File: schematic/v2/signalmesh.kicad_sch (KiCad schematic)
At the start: 164 parts, among them J1 FPGA I/O, J10 INA219_CONFIG, J11 INA219_CONFIG, J12 AAM_DBG, J13 UUM_DBG, J14 ACM_DBG, J15 INA219_CONFIG, J16 DSM_DBG, J17 LCD_display, J18 LCD_display, J19 AudioJack3, J2 FPGA I/O, J20 USB3_A, J21 USB_A, J23 USB_A, J3 LCD_display, J4 TDM_DBG, J5 INA219_CONFIG, J6 INA219_CONFIG, J7 INA219_CONFIG, J8 FPGA I/O, J9 FPGA I/O, U1 NUCLEO-H753ZI, U10 INA219AxD, U11 INA219AxD, U12 INA219AxD, U13 INA219AxD, U14 W25Q128JVS, U15 AP2112K-3.3, U16 74HC4050D, U17 NUCLEO-H753ZI, U18 HDSP-7503, U19 HDSP-7503, U2 HDSP-7503, U20 INA219AxD, U21 74HC4050D, U22 AP2112K-3.3, U23 W25Q128JVS, U24 74HC4050D, U25 AP2112K-3.3, U26 W25Q128JVS, U27 MCP2551-I-P, U28 74LVC1G3157, U29 MCP2551-I-P, U3 NUCLEO-F303RE, U30 MCP2551-I-P, U31 MCP2551-I-P, U32 CH340G, U4 YAAJ_BluePill_Part_Like, U5 24LC256-I_SN, U6 BME280, U7 INA219AxD, U8 24LC256-I_SN, U9 NUCLEO-F446RE, Y1 Crystal

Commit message: i should really make this multiple sheets
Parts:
- added D37: LED_PWR, LED_SMD:LED_0603_1608Metric, symbol Device:LED
- added J22: USB_A, Connector_USB:USB_A_CNCTech_1001-011-01101_Horizontal, symbol Connector:USB_A
- added R56: 300, Resistor_SMD:R_0805_2012Metric_Pad1.20x1.40mm_HandSolder, symbol Device:R
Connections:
- net AAM_USB_D+: now also J22.3 (D+)
- net AAM_USB_D-: now also J22.2 (D-)
- net AAM_VDD: now also J22.1 (VBUS), R56.2
- net GND: now also D37.1 (K), J22.4 (GND)
- new net: D37.2 (A), R56.1

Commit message: removing the courtyard from the filler plots. theyre not actually components just an outline with throughholes
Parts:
- removed J20: USB3_A, Connector_USB:USB3_A_Plug_Wuerth_692112030100_Horizontal, symbol Connector:USB3_A
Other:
- note added: "MEDIA USB2.0 INPUT"
- moved on the sheet: D32, J21, R50
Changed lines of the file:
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@@
 	)
 	(rectangle
-		(start 332.74 173.99)
-		(end 377.19 209.55)
+		(start 180.34 232.41)
+		(end 224.79 267.97)
 		(stroke
 			(width 0)
@@
 		)
 	)
-	(text "MIDI USB2.0 INPUT"
+	(text "MEDIA USB2.0 INPUT"
 		(exclude_from_sim no)
 		(at 355.6 449.072 0)
@@
 	(text "MIDI USB2.0 INPUT"
 		(exclude_from_sim no)
-		(at 354.33 176.022 0)
+		(at 201.93 234.442 0)
 		(effects
 			(font
@@
 	)
 	(junction
-		(at 359.41 186.69)
+		(at 207.01 245.11)
 		(diameter 0)
 		(color 0 0 0 0)
@@
 	)
 	(junction
-		(at 349.25 203.2)
+		(at 196.85 261.62)
 		(diameter 0)
 		(color 0 0 0 0)
@@
 	(wire
 		(pts
-			(xy 349.25 203.2) (xy 349.25 201.93)
+			(xy 196.85 261.62) (xy 196.85 260.35)
 		)
 		(stroke
@@
 	(wire
 		(pts
-			(xy 337.82 203.2) (xy 337.82 200.66)
+			(xy 185.42 261.62) (xy 185.42 259.08)
 		)
 		(stroke
@@
 	(wire
 		(pts
-			(xy 349.25 203.2) (xy 337.82 203.2)
+			(xy 196.85 261.62) (xy 185.42 261.62)
 		)
 		(stroke
@@
 	(wire
 		(pts
-			(xy 359.41 181.61) (xy 359.41 186.69)
+			(xy 207.01 240.03) (xy 207.01 245.11)
 		)
 		(stroke
@@
 	(wire
 		(pts
-			(xy 359.41 186.69) (xy 356.87 186.69)
+			(xy 207.01 245.11) (xy 204.47 245.11)
 		)
 		(stroke
@@
 	(wire
 		(pts
-			(xy 359.41 181.61) (xy 337.82 181.61)
+			(xy 207.01 240.03) (xy 185.42 240.03)
 		)
 		(stroke
@@
 	(wire
 		(pts
-			(xy 337.82 181.61) (xy 337.82 185.42)
+			(xy 185.42 240.03) (xy 185.42 243.84)
 		)
 		(stroke
@@
 	(wire
 		(pts
-			(xy 359.41 186.69) (xy 361.95 186.69)
+			(xy 207.01 245.11) (xy 209.55 245.11)
 		)
 		(stroke
@@
 	(global_label "AAM_USB_D-"
 		(shape bidirectional)
-		(at 356.87 194.31 0)
+		(at 204.47 252.73 0)
 		(fields_autoplaced yes)
 		(effects
@@
 		)
 		(property "Intersheetrefs" "${INTERSHEET_REFS}"
-			(at 373.1827 194.31 0)
+			(at 220.7827 252.73 0)
 			(effects
 				(font
@@
 	(global_label "AAM_USB_D+"
 		(shape bidirectional)
-		(at 356.87 191.77 0)
+		(at 204.47 250.19 0)
 		(fields_autoplaced yes)
 		(effects
@@
 		)
 		(property "Intersheetrefs" "${INTERSHEET_REFS}"
-			(at 373.1827 191.77 0)
+			(at 220.7827 250.19 0)
 			(effects
 				(font
@@
 	(global_label "AAM_VDD"
 		(shape input)
-		(at 361.95 186.69 0)
+		(at 209.55 245.11 0)
 		(fields_autoplaced yes)
 		(effects
@@
 		)
 		(property "Intersheetrefs" "${INTERSHEET_REFS}"
-			(at 373.16 186.69 0)
+			(at 220.76 245.11 0)
 			(effects
 				(font
@@
 	(symbol
 		(lib_id "Connector:USB_A")
-		(at 349.25 191.77 0)
+		(at 196.85 250.19 0)
 		(unit 1)
 		(exclude_from_sim no)
@@
 		(fields_autoplaced yes)
 		(property "Reference" "J21"
-			(at 349.25 179.07 0)
+			(at 196.85 237.49 0)
 			(effects
 				(font
@@
 		)
 		(property "Value" "USB_A"
-			(at 349.25 181.61 0)
+			(at 196.85 240.03 0)
 			(effects
 				(font
@@
 		)
 		(property "Footprint" "Connector_USB:USB_A_CNCTech_1001-011-01101_Horizontal"
-			(at 353.06 193.04 0)
+			(at 200.66 251.46 0)
 			(effects
 				(font
@@
 		)
 		(property "Datasheet" "~"
-			(at 353.06 193.04 0)
+			(at 200.66 251.46 0)
 			(effects
 				(font
@@
 		)
 		(property "Description" "USB Type A connector"
-			(at 349.25 191.77 0)
+			(at 196.85 250.19 0)
 			(effects
 				(font
@@
 	(symbol
 		(lib_id "power:GND")
-		(at 349.25 203.2 0)
+		(at 196.85 261.62 0)
 		(unit 1)
 		(exclude_from_sim no)
@@
 		(fields_autoplaced yes)
 		(property "Reference" "#PWR0132"
-			(at 349.25 209.55 0)
+			(at 196.85 267.97 0)
 			(effects
 				(font
@@
 		)
 		(property "Value" "GND"
-			(at 349.25 208.28 0)
+			(at 196.85 266.7 0)
 			(effects
 				(font
@@
 		)
 		(property "Footprint" ""
-			(at 349.25 203.2 0)
+			(at 196.85 261.62 0)
 			(effects
 				(font
@@
 		)
 		(property "Datasheet" ""
-			(at 349.25 203.2 0)
+			(at 196.85 261.62 0)
 			(effects
 				(font
@@
 		)
 		(property "Description" "Power symbol creates a global label with name \"GND\" , ground"
-			(at 349.25 203.2 0)
+			(at 196.85 261.62 0)
 			(effects
 				(font
@@
 	)
 	(symbol
-		(lib_id "Connector:USB3_A")
-		(at 38.1 93.98 0)
-		(unit 1)
-		(exclude_from_sim no)
-		(in_bom yes)
-		(on_board yes)
-		(dnp no)
-		(fields_autoplaced yes)
-		(property "Reference" "J20"
-			(at 38.1 74.93 0)
-			(effects
-				(font
-					(size 1.27 1.27)
-				)
-			)
-		)
-		(property "Value" "USB3_A"
-			(at 38.1 77.47 0)
-			(effects
-				(font
-					(size 1.27 1.27)
-				)
-			)
-		)
-		(property "Footprint" "Connector_USB:USB3_A_Plug_Wuerth_692112030100_Horizontal"
-			(at 41.91 91.44 0)
-			(effects
-				(font
-					(size 1.27 1.27)
-				)
-				(hide yes)
-			)
-		)
-		(property "Datasheet" "~"
-			(at 41.91 91.44 0)
-			(effects
-				(font
-					(size 1.27 1.27)
-				)
-				(hide yes)
-			)
-		)
-		(property "Description" "USB 3.0 A connector"
-			(at 38.1 93.98 0)
-			(effects
-				(font
-					(size 1.27 1.27)
-				)
-				(hide yes)
-			)
-		)
-		(pin "6"
-		)
-		(pin "9"
-		)
-		(pin "1"
-		)
-		(pin "2"
-		)
-		(pin "3"
-		)
-		(pin "5"
-		)
-		(pin "4"
-		)
-		(pin "7"
-		)
-		(pin "10"
-		)
-		(pin "8"
-		)
-		(instances
-			(project ""
-				(path "/fe7b15e9-f0ed-4338-9f03-dd7651dace13"
-					(reference "J20")
-					(unit 1)
-				)
-			)
-		)
-	)
-	(symbol
 		(lib_id "Device:C_Small")
 		(at 593.09 29.21 90)
@@
 	(symbol
 		(lib_id "Device:R")
-		(at 337.82 189.23 180)
+		(at 185.42 247.65 180)
 		(unit 1)
 		(exclude_from_sim no)
@@
 		(fields_autoplaced yes)
 		(property "Reference" "R50"
-			(at 340.36 187.9599 0)
+			(at 187.96 246.3799 0)
 			(effects
 				(font
@@
 		)
 		(property "Value" "300"
-			(at 340.36 190.4999 0)
+			(at 187.96 248.9199 0)
 			(effects
 				(font
@@
 		)
 		(property "Footprint" "Resistor_SMD:R_0805_2012Metric_Pad1.20x1.40mm_HandSolder"
-			(at 339.598 189.23 90)
+			(at 187.198 247.65 90)
 			(effects
 				(font
@@
 		)
 		(property "Datasheet" "~"
-			(at 337.82 189.23 0)
+			(at 185.42 247.65 0)
 			(effects
 				(font
@@
 		)
 		(property "Description" "Resistor"
-			(at 337.82 189.23 0)
+			(at 185.42 247.65 0)
 			(effects
 				(font
@@
 		)
 		(property "DigiKey_Part_Number" "311-10.0KCRCT-ND"
-			(at 337.82 189.23 0)
+			(at 185.42 247.65 0)
 			(effects
 				(font
@@
 		)
 		(property "Price" "0.0129"
-			(at 337.82 189.23 0)
+			(at 185.42 247.65 0)
 			(effects
 				(font
@@
 	(symbol
 		(lib_id "Device:LED")
-		(at 337.82 196.85 90)
+		(at 185.42 255.27 90)
 		(unit 1)
 		(exclude_from_sim no)
@@
 		(fields_autoplaced yes)
 		(property "Reference" "D32"
-			(at 341.63 197.1674 90)
+			(at 189.23 255.5874 90)
 			(effects
 				(font
@@
 		)
 		(property "Value" "LED_PWR"
-			(at 341.63 199.7074 90)
+			(at 189.23 258.1274 90)
 			(effects
 				(font
@@
 		)
 		(property "Footprint" "LED_SMD:LED_0603_1608Metric"
-			(at 337.82 196.85 0)
+			(at 185.42 255.27 0)
 			(effects
 				(font
@@
 		)
 		(property "Datasheet" "~"
-			(at 337.82 196.85 0)
+			(at 185.42 255.27 0)
 			(effects
 				(font
@@
 		)
 		(property "Description" "Light emitting diode"
-			(at 337.82 196.85 0)
+			(at 185.42 255.27 0)
 			(effects
 				(font
@@
 		)
 		(property "Sim.Pins" "1=K 2=A"
-			(at 337.82 196.85 0)
+			(at 185.42 255.27 0)
 			(effects
 				(font

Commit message: moving to multiple sheets for the schematic
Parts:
- removed C11, C12, C13: 22pf, Capacitor_SMD:C_0805_2012Metric, symbol Device:C_Small
- removed D15, D21, D32, D33, D34, D37: LED_PWR, LED_SMD:LED_0603_1608Metric, symbol Device:LED
- removed D16, D22: LED_OK, LED_SMD:LED_0603_1608Metric, symbol Device:LED
- removed D17, D23: LED_FAIL, LED_SMD:LED_0603_1608Metric, symbol Device:LED
- removed D18, D24: LED_WARN, LED_SMD:LED_0603_1608Metric, symbol Device:LED
- removed D35: TXD, LED_SMD:LED_0603_1608Metric, symbol Device:LED
- removed D36: RXD, LED_SMD:LED_0603_1608Metric, symbol Device:LED
- removed J12: AAM_DBG, Connector_PinHeader_1.00mm:PinHeader_1x03_P1.00mm_Horizontal, symbol Connector_Generic:Conn_01x03
- removed J16: DSM_DBG, Connector_PinHeader_1.00mm:PinHeader_1x03_P1.00mm_Horizontal, symbol Connector_Generic:Conn_01x03
- removed J17, J3: LCD_display, Connector_PinHeader_1.00mm:PinHeader_1x04_P1.00mm_Vertical_SMD_Pin1Left, symbol Connector_Generic:Conn_01x04
- removed J19: AudioJack3, Connector_Audio:Jack_3.5mm_CUI_SJ-3523-SMT_Horizontal, symbol Connector_Audio:AudioJack3
- removed J21, J22, J23: USB_A, Connector_USB:USB_A_CNCTech_1001-011-01101_Horizontal, symbol Connector:USB_A
- removed R38, R39, R40, R41, R5, R50, R51, R52, R53, R54, R56, R6, R7, R8: 300, Resistor_SMD:R_0805_2012Metric_Pad1.20x1.40mm_HandSolder, symbol Device:R
- removed R55: 1k5, Resistor_SMD:R_0805_2012Metric_Pad1.20x1.40mm_HandSolder, symbol Device:R
- removed U1, U17: NUCLEO-H753ZI, NUCLEO-H753ZI:MODULE_NUCLEO-H753ZI, symbol NUCLEO-H753ZI:NUCLEO-H753ZI
- removed U32: CH340G, Package_SO:SOIC-16_3.9x9.9mm_P1.27mm, symbol Interface_USB:CH340G
- removed Y1: Crystal, symbol Device:Crystal
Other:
- added sheet AAM (AAM.kicad_sch)
- added sheet DSM (DSM.kicad_sch)
- note removed: "AAM USB2.0 DBG PORT"
- note removed: "MEDIA USB2.0 INPUT"
- note removed: "MIDI USB2.0 INPUT"
- note removed: "STM32H753 NUCLEO"
- note removed: "STM32H755 NUCLEO"

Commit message: should probably write some code now
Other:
- note removed: "Data Siphon Module"
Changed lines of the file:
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@@
 	)
 	(rectangle
-		(start 346.71 274.32)
-		(end 393.7 288.29)
+		(start 350.52 299.72)
+		(end 397.51 313.69)
 		(stroke
 			(width 0)
@@
 	)
 	(rectangle
-		(start 76.2 292.1)
-		(end 388.62 495.3)
-		(stroke
-			(width 0)
-			(type solid)
-		)
-		(fill
-			(type none)
-		)
-	)
-	(rectangle
 		(start 629.92 21.59)
 		(end 684.53 62.23)
@@
 	)
 	(rectangle
-		(start 77.47 297.18)
-		(end 378.46 444.5)
-		(stroke
-			(width 0)
-			(type solid)
-		)
-		(fill
-			(type none)
-		)
-	)
-	(rectangle
 		(start 629.92 62.23)
 		(end 684.53 102.87)
@@
 	(text "AAM -> DSM Record"
 		(exclude_from_sim no)
-		(at 382.778 275.844 0)
+		(at 386.588 301.244 0)
 		(effects
 			(font
@@
 		)
 	)
-	(text "Data Siphon Module"
-		(exclude_from_sim no)
-		(at 369.824 294.894 0)
-		(effects
-			(font
-				(size 1.905 1.905)
-			)
-		)
-	)
 	(text "DSM CAN TLM"
 		(exclude_from_sim no)
@@
 	(wire
 		(pts
-			(xy 374.65 283.21) (xy 365.76 283.21)
+			(xy 378.46 308.61) (xy 369.57 308.61)
 		)
 		(stroke
@@
 	(wire
 		(pts
-			(xy 374.65 280.67) (xy 365.76 280.67)
+			(xy 378.46 306.07) (xy 369.57 306.07)
 		)
 		(stroke
@@
 	(wire
 		(pts
-			(xy 374.65 278.13) (xy 365.76 278.13)
+			(xy 378.46 303.53) (xy 369.57 303.53)
 		)
 		(stroke
@@
 	(wire
 		(pts
-			(xy 374.65 285.75) (xy 365.76 285.75)
+			(xy 378.46 311.15) (xy 369.57 311.15)
 		)
 		(stroke
@@
 	(global_label "DSM_DAC_R"
 		(shape bidirectional)
-		(at 374.65 283.21 0)
+		(at 378.46 308.61 0)
 		(fields_autoplaced yes)
 		(effects
@@
 		)
 		(property "Intersheetrefs" "${INTERSHEET_REFS}"
-			(at 389.5112 283.21 0)
+			(at 393.3212 308.61 0)
 			(effects
 				(font
@@
 	(global_label "AAM_INTRPT_RX"
 		(shape bidirectional)
-		(at 365.76 278.13 180)
+		(at 369.57 303.53 180)
 		(fields_autoplaced yes)
 		(effects
@@
 		)
 		(property "Intersheetrefs" "${INTERSHEET_REFS}"
-			(at 347.2097 278.13 0)
+			(at 351.0197 303.53 0)
 			(effects
 				(font
@@
 	(global_label "DSM_INTRPT_TX"
 		(shape bidirectional)
-		(at 374.65 278.13 0)
+		(at 378.46 303.53 0)
 		(fields_autoplaced yes)
 		(effects
@@
 		)
 		(property "Intersheetrefs" "${INTERSHEET_REFS}"
-			(at 393.2002 278.13 0)
+			(at 397.0102 303.53 0)
 			(effects
 				(font
@@
 	(global_label "DSM_INTRPT_RX"
 		(shape bidirectional)
-		(at 374.65 280.67 0)
+		(at 378.46 306.07 0)
 		(fields_autoplaced yes)
 		(effects
@@
 		)
 		(property "Intersheetrefs" "${INTERSHEET_REFS}"
-			(at 393.5026 280.67 0)
+			(at 397.3126 306.07 0)
 			(effects
 				(font
@@
 	(global_label "AAM_INTRPT_TX"
 		(shape bidirectional)
-		(at 365.76 280.67 180)
+		(at 369.57 306.07 180)
 		(fields_autoplaced yes)
 		(effects
@@
 		)
 		(property "Intersheetrefs" "${INTERSHEET_REFS}"
-			(at 347.5121 280.67 0)
+			(at 351.3221 306.07 0)
 			(effects
 				(font
@@
 	(global_label "AAM_DAC_L"
 		(shape bidirectional)
-		(at 365.76 285.75 180)
+		(at 369.57 311.15 180)
 		(fields_autoplaced yes)
 		(effects
@@
 		)
 		(property "Intersheetrefs" "${INTERSHEET_REFS}"
-			(at 351.443 285.75 0)
+			(at 355.253 311.15 0)
 			(effects
 				(font
@@
 	(global_label "DSM_DAC_L"
 		(shape bidirectional)
-		(at 374.65 285.75 0)
+		(at 378.46 311.15 0)
 		(fields_autoplaced yes)
 		(effects
@@
 		)
 		(property "Intersheetrefs" "${INTERSHEET_REFS}"
-			(at 389.2693 285.75 0)
+			(at 393.0793 311.15 0)
 			(effects
 				(font
@@
 	(global_label "AAM_DAC_R"
 		(shape bidirectional)
-		(at 365.76 283.21 180)
+		(at 369.57 308.61 180)
 		(fields_autoplaced yes)
 		(effects
@@
 		)
 		(property "Intersheetrefs" "${INTERSHEET_REFS}"
-			(at 351.2011 283.21 0)
+			(at 355.0111 308.61 0)
 			(effects
 				(font
@@
 	)
 	(sheet
-		(at 340.36 212.09)
+		(at 368.3 292.1)
 		(size 12.7 3.81)
 		(exclude_from_sim no)
@@
 		)
 		(property "Sheetname" "AAM"
-			(at 340.36 211.3784 0)
+			(at 368.3 291.3884 0)
 			(effects
 				(font
@@
 		)
 		(property "Sheetfile" "AAM.kicad_sch"
-			(at 340.36 216.4846 0)
+			(at 368.3 296.4946 0)
 			(effects
 				(font
@@
 	)
 	(sheet
-		(at 388.62 411.48)
-		(size 12.7 17.78)
+		(at 368.3 317.5)
+		(size 12.7 3.81)
 		(exclude_from_sim no)
 		(in_bom yes)
@@
 		)
 		(property "Sheetname" "DSM"
-			(at 388.62 410.7684 0)
+			(at 368.3 316.7884 0)
 			(effects
 				(font
@@
 		)
 		(property "Sheetfile" "DSM.kicad_sch"
-			(at 388.62 429.8446 0)
+			(at 368.3 321.8946 0)
 			(effects
 				(font

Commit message: adding more sheets in the schematic
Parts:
- removed D19: LED_PWR, LED_SMD:LED_0603_1608Metric, symbol Device:LED
- removed R1: 300, Resistor_SMD:R_0805_2012Metric_Pad1.20x1.40mm_HandSolder, symbol Device:R
- removed U18, U19, U2: HDSP-7503, Display_7Segment:HDSP-A151, symbol Display_Character:HDSP-7503
- removed U4: YAAJ_BluePill_Part_Like, Footprints:YAAJ_WeAct_BlackPill_SWD_2, symbol YAAJ_BluePill_Part_Like:YAAJ_BluePill_Part_Like
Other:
- note removed: "7-Segment Display Driver (7SDD)"
- note removed: "Audio Acquisition Module"
- note removed: "Driver MCU for a 3 digit 7 segment display.Ideally audio engine settings can be displayed through here live"

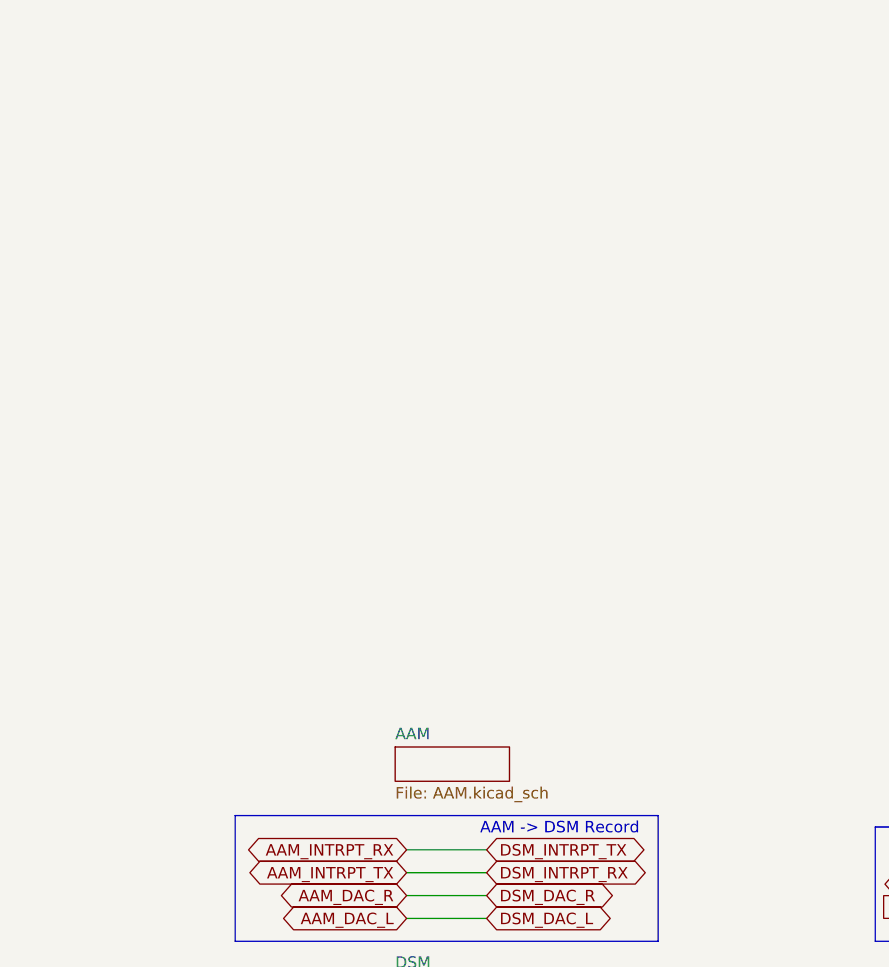
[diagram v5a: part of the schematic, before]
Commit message: progress on putting things in different sheets
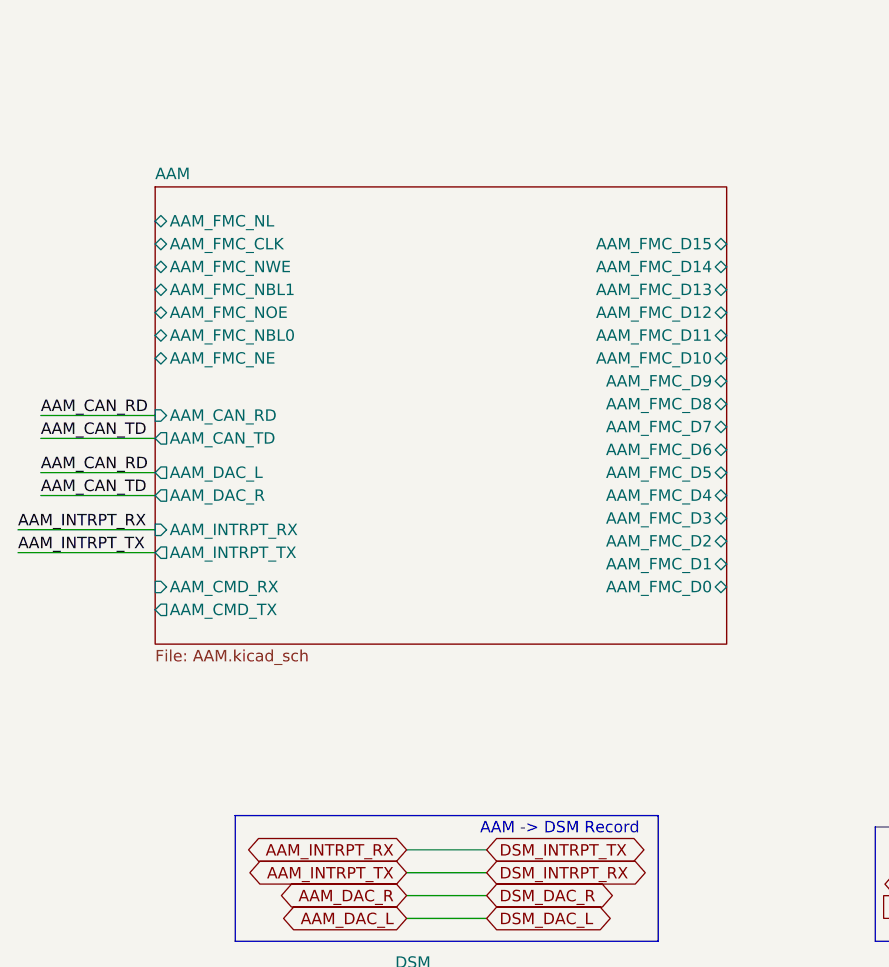
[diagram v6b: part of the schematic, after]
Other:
- sheet AAM ports: added AAM_CAN_RD, AAM_CAN_TD, AAM_CMD_RX, AAM_CMD_TX, AAM_DAC_L, AAM_DAC_R, AAM_FMC_CLK, AAM_FMC_D0, AAM_FMC_D1, AAM_FMC_D10, AAM_FMC_D11, AAM_FMC_D12, AAM_FMC_D13, AAM_FMC_D14, AAM_FMC_D15, AAM_FMC_D2, AAM_FMC_D3, AAM_FMC_D4, AAM_FMC_D5, AAM_FMC_D6, AAM_FMC_D7, AAM_FMC_D8, AAM_FMC_D9, AAM_FMC_NBL0, AAM_FMC_NBL1, AAM_FMC_NE, AAM_FMC_NL, AAM_FMC_NOE, AAM_FMC_NWE, AAM_INTRPT_RX, AAM_INTRPT_TX; removed none

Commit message: v2 updates. remove sniffer
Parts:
- removed D11: LED_PWR, LED_SMD:LED_0603_1608Metric, symbol Device:LED
- removed D12: LED_OK, LED_SMD:LED_0603_1608Metric, symbol Device:LED
- removed D13: LED_FAIL, LED_SMD:LED_0603_1608Metric, symbol Device:LED
- removed D14: LED_WARN, LED_SMD:LED_0603_1608Metric, symbol Device:LED
- removed J1, J2, J8, J9: FPGA I/O, Connector_PinSocket_2.54mm:PinSocket_1x24_P2.54mm_Vertical, symbol Connector_Generic:Conn_01x24
- removed R34, R35, R36, R37: 300, Resistor_SMD:R_0805_2012Metric_Pad1.20x1.40mm_HandSolder, symbol Device:R
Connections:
- net 5V_AAM renamed 5V_APM
- net AAM_CAN_RD renamed APM_CAN_RD
- net AAM_CAN_TD renamed APM_CAN_TD
- net VDD_AAM renamed VDD_APM
- no-connect marks 11 -> 0
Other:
- sheet AAM renamed APM
- added sheet ACM (ACM.kicad_sch)
- sheet APM: file AAM.kicad_sch -> APM.kicad_sch
- sheet APM ports: added APM_CAN_RD, APM_CAN_TD, APM_CMD_RX, APM_CMD_TX, APM_DAC_L, APM_DAC_R, APM_INTRPT_RX, APM_INTRPT_TX; removed AAM_CAN_RD, AAM_CAN_TD, AAM_CMD_RX, AAM_CMD_TX, AAM_DAC_L, AAM_DAC_R, AAM_FMC_CLK, AAM_FMC_D0, AAM_FMC_D1, AAM_FMC_D10, AAM_FMC_D11, AAM_FMC_D12, AAM_FMC_D13, AAM_FMC_D14, AAM_FMC_D15, AAM_FMC_D2, AAM_FMC_D3, AAM_FMC_D4, AAM_FMC_D5, AAM_FMC_D6, AAM_FMC_D7, AAM_FMC_D8, AAM_FMC_D9, AAM_FMC_NBL0, AAM_FMC_NBL1, AAM_FMC_NE, AAM_FMC_NL, AAM_FMC_NOE, AAM_FMC_NWE, AAM_INTRPT_RX, AAM_INTRPT_TX
- sheet DSM ports: added DSM_CAN_RD, DSM_CAN_TD, DSM_DAC_L, DSM_DAC_R, DSM_FMC_CLK, DSM_FMC_D0, DSM_FMC_D1, DSM_FMC_D10, DSM_FMC_D11, DSM_FMC_D12, DSM_FMC_D13, DSM_FMC_D14, DSM_FMC_D15, DSM_FMC_D2, DSM_FMC_D3, DSM_FMC_D4, DSM_FMC_D5, DSM_FMC_D6, DSM_FMC_D7, DSM_FMC_D8, DSM_FMC_D9, DSM_FMC_NBL0, DSM_FMC_NBL1, DSM_FMC_NE, DSM_FMC_NL, DSM_FMC_NOE, DSM_FMC_NWE, DSM_INTRPT_RX, DSM_INTRPT_TX; removed none
- note added: "APM <-> ACM FMC bus"
- note added: "APM <-> ACM cmd ctrl"
- note added: "APM CAN TLM"
- note added: "INA219 APM"
- note removed: "AAM -> DSM Record"
- note removed: "AAM <-> ACM FMC bus"
- note removed: "AAM <-> ACM cmd ctrl"
- note removed: "AAM CAN TLM"
- note removed: "Audio Creation Module"
- note removed: "INA219 AAM"
- note removed: "Tang Nano 9k FPGA"
